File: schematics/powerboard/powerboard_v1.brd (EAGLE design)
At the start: 50 x 50 mm, 39 parts, among them IC1 ACS756LCB-100B-PFF-T, IC2 ATMEGA644-A, Y1 10MHZ

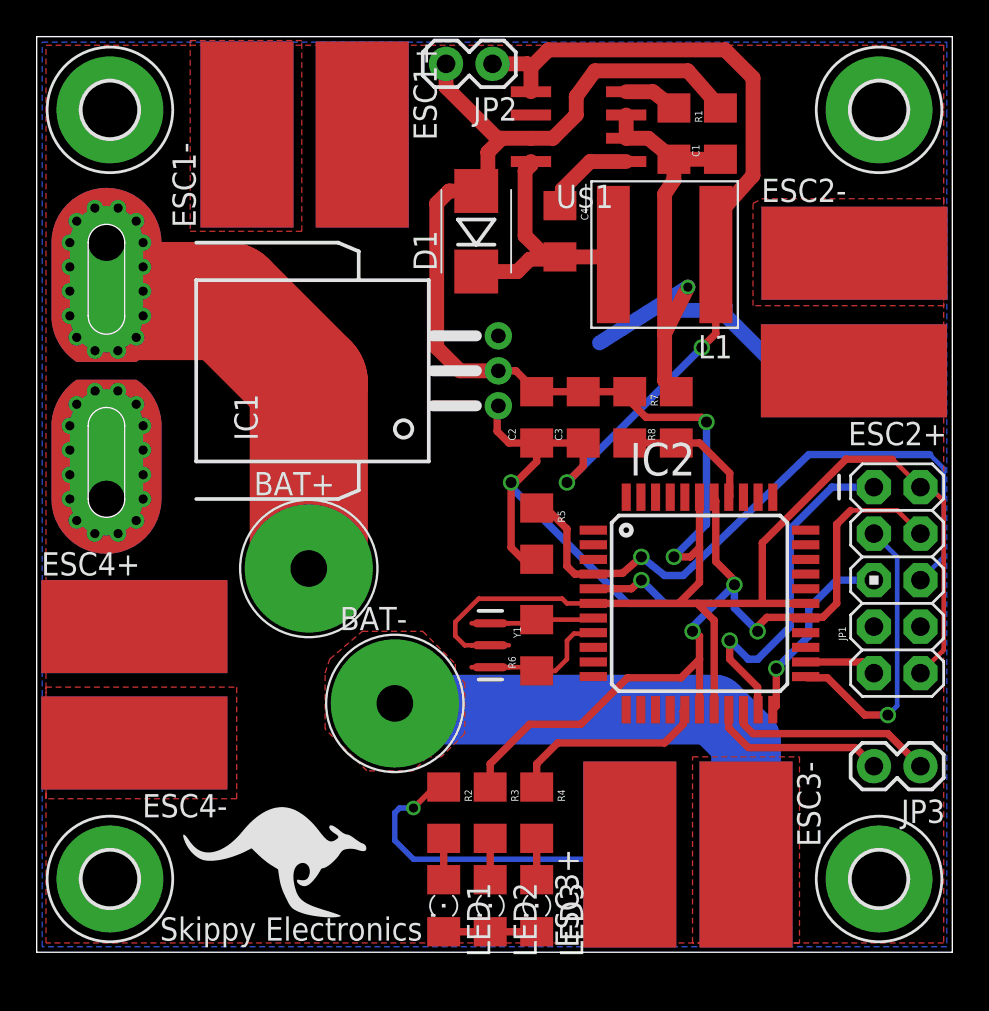
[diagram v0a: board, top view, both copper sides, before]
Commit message: Removed old powerboard revs
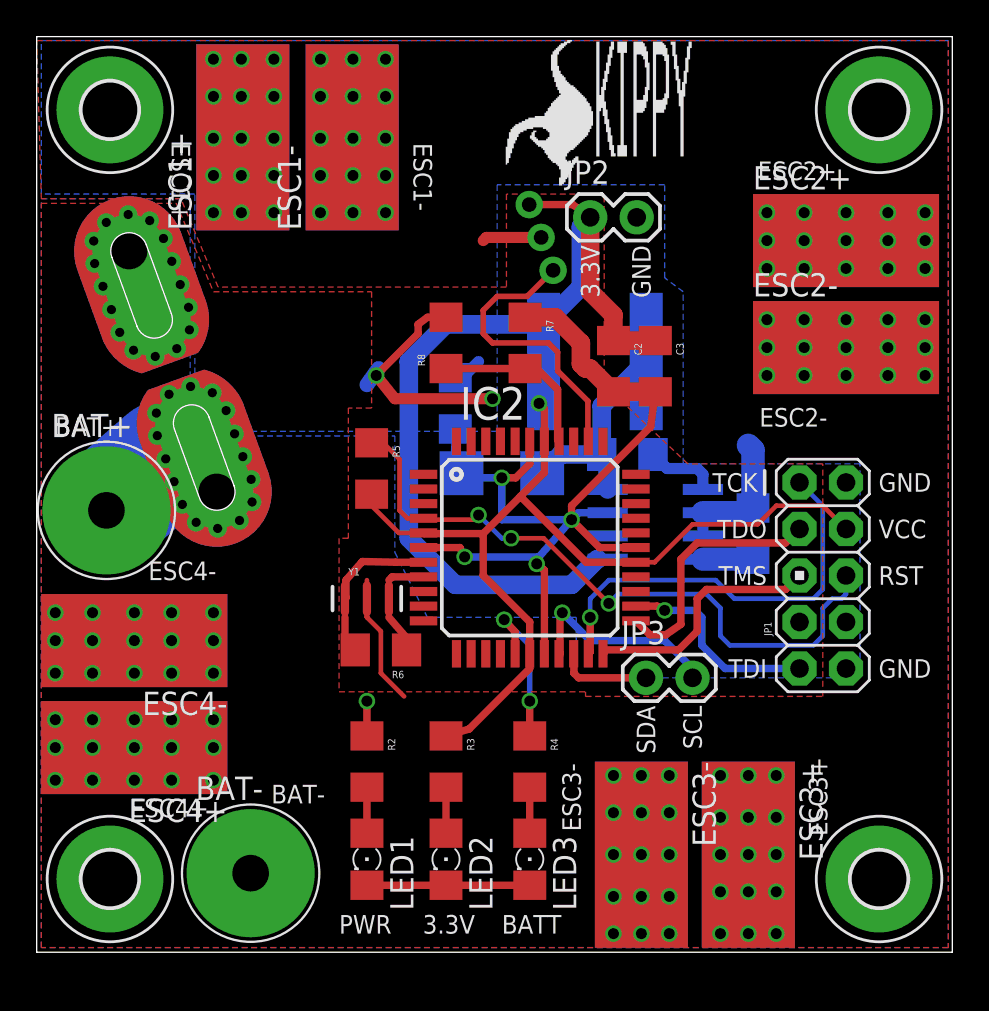
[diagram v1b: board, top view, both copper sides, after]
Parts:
- removed PLC1: SKIPPY-PLC-10MMPLC, skippy-logo:SKIPPY-PLC-10MM
- added U$2: SKIPPYTXT-PLC-10MM, skippy-logo:SKIPPYTXT-PLC-10MM
- moved R1 22.3 mm to (39.1, 22.9), flipped to the bottom, turned to 90 degrees
- moved U$1 22.1 mm to (33.8, 23.4), flipped to the bottom, turned to 270 degrees
- moved C1 20.7 mm to (22.9, 30.0), flipped to the bottom, turned to 270 degrees
- moved JP3 15.7 mm to (33.3, 15.0), turned to 0 degrees
- moved D1 13.3 mm to (25.4, 26.2), flipped to the bottom, turned to 0 degrees
- moved R8 13.2 mm to (22.4, 33.3)
- moved C4 12.7 mm to (32.3, 27.2), flipped to the bottom, turned to 0 degrees
- moved BAT- 12.2 mm to (11.7, 4.32)
- moved BAT+ 11.5 mm to (3.81, 24.1)
- moved JP2 9.94 mm to (30.2, 40.1), turned to 0 degrees
- moved IC2 9.76 mm to (26.9, 22.1)
- moved R5 9.69 mm to (18.3, 26.4)
- moved R6 8.51 mm to (18.8, 16.5), turned to 180 degrees
- moved Y1 7.19 mm to (18.0, 19.3), turned to 0 degrees
- moved ESC2+ 7.13 mm to (44.2, 38.9), turned to 270 degrees
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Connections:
- new net I_VOUT: IC1.3, IC2.35
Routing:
- net GND: track 152.3 -> 86.6 mm, vias 2 -> 64
- net N$1: track 22.9 -> 4.29 mm
- net 3.3V: track 124.8 -> 106.5 mm, vias 7 -> 1
- net I_VOUT: track 0.00 -> 16.0 mm
- net V_BATT: track 61.5 -> 51.3 mm, vias 2 -> 63
- net TDI: track 3.98 -> 11.2 mm, vias 0 -> 1
- net SDA: track 11.4 -> 5.11 mm
- net TCK: track 19.7 -> 23.2 mm
- net TMS: track 10.5 -> 13.6 mm, vias 1 -> 0
- net N$8: track 4.73 -> 7.71 mm
- net TDO: track 16.0 -> 13.7 mm, vias 1 -> 0
- net N$2: track 13.9 -> 11.8 mm
- net LO_BATT_LED: track 11.0 -> 9.02 mm, vias 0 -> 2
- net N$10: track 7.48 -> 9.44 mm
- net N$9: track 6.16 -> 4.34 mm
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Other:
- board text added: "3.3V"
- board text added: "BAT+"
- board text added: "BAT-"
- board text added: "BATT"
- board text added: "ESC1+"
- board text added: "ESC1-"
- board text added: "ESC2+"
- board text added: "ESC2-"
- board text added: "ESC3+"
- board text added: "ESC3-"
- board text added: "ESC4+"
- board text added: "ESC4-"
- board text added: "GND"
- board text added: "PWR"
- board text added: "RST"
- board text added: "SCL"
- board text added: "SDA"
- board text added: "TCK"
- board text added: "TDI"
- board text added: "TDO"
- board text added: "TMS"
- board text added: "VCC"
